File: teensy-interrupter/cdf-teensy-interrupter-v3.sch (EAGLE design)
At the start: 42 parts, among them IC1 TP4056, Q1 BC817-40LT1SMD

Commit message: More work
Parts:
- removed MIDI, PULSE: 100SP1T1B4M2QE, keves:100SP1T1B4M2QE
- removed PULSE_DUTY, PULSE_WIDTH: 10K PTV09A-4025F-B103, Bourns:POTENTIOMETERPTV09A_VERTICAL
- removed SW1: (no value), adafruit:DPDT-EG1390
- added D1, D3: 1A/23V/620mV, SparkFun-DiscreteSemi:DIODE-SCHOTTKY-BAT20J
- added PWR: 100SP1T1B4M2QE, keves:100SP1T1B4M2QE
- added R12: 50000, rcl:R-US_R0805
- added R13: 100000, rcl:R-US_R0805
- added S1: ENCODER-2LED, SparkFun-Switches:ENCODER-2LED
- R3, R5: value 330 -> 100
- R7: value 68 -> 27
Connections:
- net RX renamed MIDI_RX
- removed net PULSE_DUTY: PULSE_DUTY.WIPER, U$1.15/A1/T
- removed net PULSE_WIDTH: PULSE_WIDTH.WIPER, U$1.14/A1
- removed net TX2: U$1.22/A8/T/PWM
- removed net TX3: U$1.23/A9/T/PWM
- new net ENC_A: S1.A, U$1.14/A1
- new net ENC_B: S1.B, U$1.15/A1/T
- new net ENC_Z: S1.SW, U$1.16/A2/T
- new net N$23: B+.1, D3.A, IC1.BAT
- new net V_SENSE: R12.1, R13.2
- net +3V3: now also R5.2, S1.C, U$3.VDD; no longer MIDI.1, PULSE.1, PULSE_DUTY.CW, PULSE_WIDTH.CW
- net +5V: now also VR1.CCW; no longer R3.2, R5.2, R7.2, U$3.VDD, VR1.CW
- net GND: now also R13.1, VR1.CW; no longer MIDI.3, PULSE.3, PULSE_DUTY.CCW, PULSE_WIDTH.CCW, VR1.CCW
- net MIDI_MODE: no longer MIDI.2
- net N$20: now also D1.C, D3.C, PWR.2; no longer B+.1, IC1.BAT, SW11.S, SW12.O
- net N$22: now also D1.A, VUSB.1; no longer SW11.P
- net N$24: now also R3.2, R7.2; no longer SW11.O, SW12.S, VUSB.1
- net PULSE_MODE: no longer PULSE.2
- net V+: now also PWR.3, R12.2; no longer SW12.P
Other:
- moved on the sheet: B+, B-, C1, C2, C3, CHARGED, CHARGING, D2, EMERGENCY, IC1, LED_POWER, LED_TX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

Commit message: WIP?
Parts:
- removed B+, B-: (no value), adafruit:PINHD-1X1
- removed EMERGENCY: TL1105LF250Q, SparkFun-Electromechanical:SWITCH-MOMENTARY-2PTH
- removed R4: 220, rcl:R-US_0204/7
- removed U$3: LCD-HD447804-HOLES16X2-4-HOLES, HD44780LCD:LCD-HD447804-HOLES16X2-4-HOLES
- removed VR1: 10k, SparkFun-Resistors:TRIMPOT-PTH-10MM-KNOB-1/2W-10%
- added BATT, ESTOP: (no value), pinhead:PINHD-1X2
- added R14, R15: 100, rcl:R-US_R0805
- added SCRN: (no value), adafruit:PINHD-1X3
- renumbered U$1 to TEENSY, U$4 to MIDI
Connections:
- removed net +5V: R4.1, VR1.CCW
- removed net LCD_D4: TEENSY.5/PWM, U$3.DB4
- removed net LCD_D5: TEENSY.6/PWM, U$3.DB5
- removed net LCD_D6: TEENSY.7/RX3, U$3.DB6
- removed net LCD_D7: TEENSY.8/TX3, U$3.DB7
- removed net LCD_EN: TEENSY.4/CAN-RX-PWM, U$3.E
- removed net LCD_RS: TEENSY.3/CAN-TX/PWM, U$3.RS
- removed net MIDI_MODE: TEENSY.10/TX2/PWM
- removed net N$23: B+.1, D3.A, IC1.BAT
- removed net N$5: U$3.VO, VR1.WIPER
- removed net N$6: R4.2, U$3.A
- removed net PULSE_MODE: TEENSY.9/RX2/PWM
- new net B+: BATT.2, D3.A, IC1.BAT
- new net B+1: ESTOP.2
- new net IND_G: R15.1, TEENSY.17/A3/T
- new net IND_R: R14.1, TEENSY.18/A4/T/SDA0
- new net N$25: R15.2, S1.+G
- new net N$26: R14.2, S1.+R
- new net SCRN_TX: SCRN.1, TEENSY.1/TX1/T
- net +3V3: now also SCRN.3; no longer U$3.VDD
- net EMERGENCY: now also TEENSY.19/A5/T/SCL0; no longer EMERGENCY.1, TEENSY.11/MOSI
- net ENC_A: now also TEENSY.15/A1/T; no longer TEENSY.14/A1
- net ENC_B: now also TEENSY.14/A1; no longer TEENSY.15/A1/T
- net GND: now also BATT.1, ESTOP.1, SCRN.2; no longer B-.1, EMERGENCY.2, U$3.K, U$3.R/W, U$3.VSS, VR1.CW
- net V_SENSE: now also TEENSY.20/A6/PWM
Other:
- moved on the sheet: C1, CHARGED, CHARGING, D1, D2, D3, FB1, FB2, IC1, LED_TX, OPT1, Q1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

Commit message: v3 first press
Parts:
- removed D2: (no value), diode:DIODE-DO-214AC
- removed PWR: 100SP1T1B4M2QE, keves:100SP1T1B4M2QE
- added D4: 1A/23V/620mV, SparkFun-DiscreteSemi:DIODE-SCHOTTKY-BAT20J
- added POWER: (no value), pinhead:PINHD-1X2
- H1, H2, H3, H4: value MOUNT-HOLE3.3 -> MOUNT-PAD-ROUND3.0; device holes:MOUNT-HOLE3.3 -> holes:MOUNT-PAD-ROUND3.0
- renumbered LED_TX to TX1
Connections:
- net N$24 renamed 3.3V
- removed net B+1: ESTOP.2
- net EMERGENCY: now also ESTOP.2, TEENSY.5/PWM; no longer TEENSY.19/A5/T/SCL0
- net ENC_A: now also TEENSY.13/SCK/LED; no longer TEENSY.15/A1/T
- net GND: now also H1.MOUNT, H2.MOUNT, H3.MOUNT, H4.MOUNT
- net N$2: now also D4.C; no longer D2.C
- net N$20: now also POWER.1; no longer PWR.2
- net N$3: now also D4.A; no longer D2.A
- net V+: now also POWER.2; no longer PWR.3
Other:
- note removed: "TL1105LF250Q"
- moved on the sheet: BATT, ESTOP, H1, H2, H3, H4, R14, R15, S1, SCRN

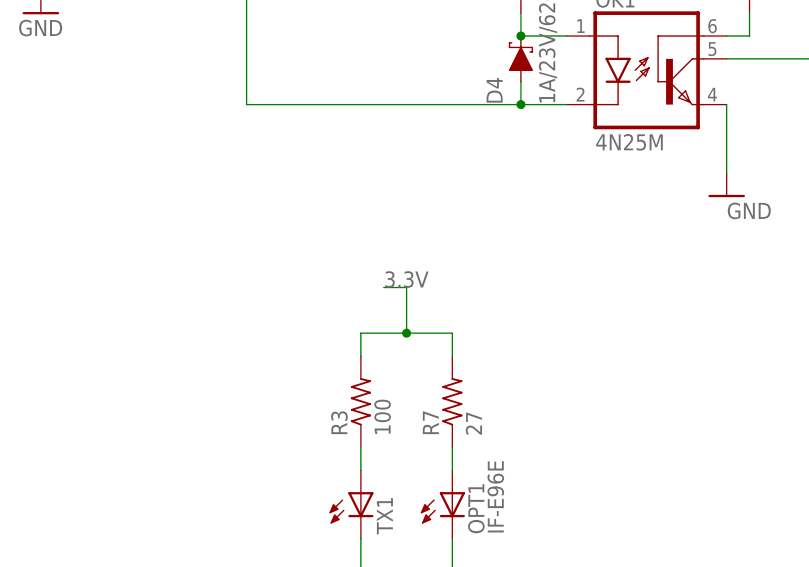
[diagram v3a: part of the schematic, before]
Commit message: Small board shrink
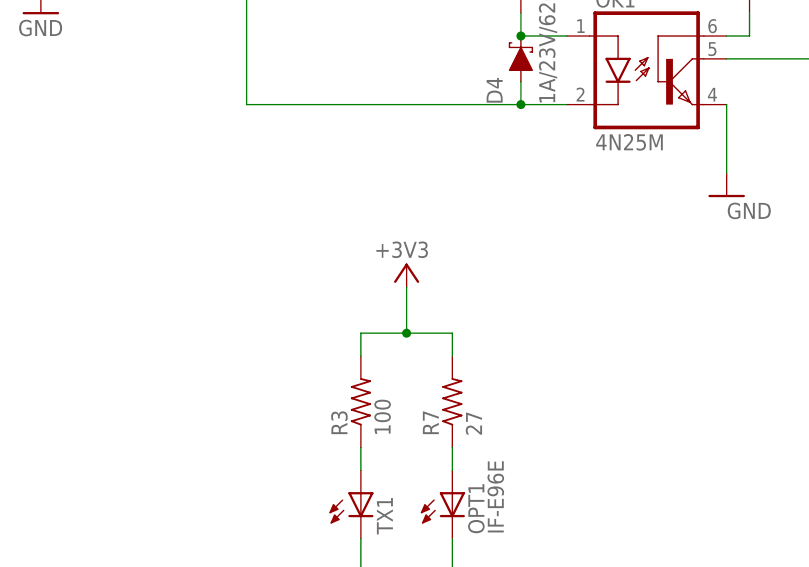
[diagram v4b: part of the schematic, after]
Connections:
- removed net 3.3V: R3.2, R7.2
- net +3V3: now also R3.2, R7.2
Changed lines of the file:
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@@
 <part name="H4" library="holes" library_urn="urn:adsk.eagle:library:237" deviceset="MOUNT-PAD-ROUND" device="3.0" package3d_urn="urn:adsk.eagle:package:14280/1"/>
 <part name="GND6" library="supply1" library_urn="urn:adsk.eagle:library:371" deviceset="GND" device=""/>
+<part name="+3V2" library="supply1" library_urn="urn:adsk.eagle:library:371" deviceset="+3V3" device=""/>
 </parts>
 <sheets>
@@
 <instance part="GND6" gate="1" x="-68.58" y="104.14" smashed="yes">
 <attribute name="VALUE" x="-71.12" y="101.6" size="1.778" layer="96"/>
+</instance>
+<instance part="+3V2" gate="G$1" x="-27.94" y="76.2" smashed="yes">
+<attribute name="VALUE" x="-25.4" y="78.74" size="1.778" layer="96" rot="R180"/>
 </instance>
 </instances>
@@
 <pinref part="+3V5" gate="G$1" pin="+3V3"/>
 <wire x1="170.18" y1="88.9" x2="170.18" y2="93.98" width="0.1524" layer="91"/>
+</segment>
+<segment>
+<wire x1="-22.86" y1="66.04" x2="-22.86" y2="68.58" width="0.1524" layer="91"/>
+<wire x1="-22.86" y1="68.58" x2="-27.94" y2="68.58" width="0.1524" layer="91"/>
+<wire x1="-27.94" y1="68.58" x2="-33.02" y2="68.58" width="0.1524" layer="91"/>
+<wire x1="-33.02" y1="68.58" x2="-33.02" y2="66.04" width="0.1524" layer="91"/>
+<pinref part="R3" gate="G$1" pin="2"/>
+<pinref part="R7" gate="G$1" pin="2"/>
+<pinref part="+3V2" gate="G$1" pin="+3V3"/>
+<wire x1="-27.94" y1="73.66" x2="-27.94" y2="68.58" width="0.1524" layer="91"/>
+<junction x="-27.94" y="68.58"/>
 </segment>
 </net>
@@
 </segment>
 </net>
-<net name="3.3V" class="0">
-<segment>
-<wire x1="-22.86" y1="66.04" x2="-22.86" y2="68.58" width="0.1524" layer="91"/>
-<wire x1="-22.86" y1="68.58" x2="-27.94" y2="68.58" width="0.1524" layer="91"/>
-<wire x1="-27.94" y1="68.58" x2="-33.02" y2="68.58" width="0.1524" layer="91"/>
-<wire x1="-33.02" y1="68.58" x2="-33.02" y2="66.04" width="0.1524" layer="91"/>
-<pinref part="R3" gate="G$1" pin="2"/>
-<pinref part="R7" gate="G$1" pin="2"/>
-<wire x1="-27.94" y1="68.58" x2="-27.94" y2="73.66" width="0.1524" layer="91"/>
-<wire x1="-27.94" y1="73.66" x2="-30.48" y2="73.66" width="0.1524" layer="91"/>
-<junction x="-27.94" y="68.58"/>
-<label x="-30.48" y="73.66" size="1.778" layer="95"/>
-</segment>
-</net>

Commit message: As printed
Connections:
- net GND: now also S1.-
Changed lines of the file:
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@@
 <part name="GND6" library="supply1" library_urn="urn:adsk.eagle:library:371" deviceset="GND" device=""/>
 <part name="+3V2" library="supply1" library_urn="urn:adsk.eagle:library:371" deviceset="+3V3" device=""/>
+<part name="GND7" library="supply1" library_urn="urn:adsk.eagle:library:371" deviceset="GND" device=""/>
 </parts>
 <sheets>
@@
 <instance part="+3V2" gate="G$1" x="-27.94" y="76.2" smashed="yes">
 <attribute name="VALUE" x="-25.4" y="78.74" size="1.778" layer="96" rot="R180"/>
+</instance>
+<instance part="GND7" gate="1" x="180.34" y="109.22" smashed="yes">
+<attribute name="VALUE" x="177.8" y="106.68" size="1.778" layer="96"/>
 </instance>
 </instances>
@@
 <pinref part="GND6" gate="1" pin="GND"/>
 </segment>
+<segment>
+<pinref part="S1" gate="G$1" pin="-"/>
+<pinref part="GND7" gate="1" pin="GND"/>
+<wire x1="177.8" y1="116.84" x2="180.34" y2="116.84" width="0.1524" layer="91"/>
+<wire x1="180.34" y1="116.84" x2="180.34" y2="111.76" width="0.1524" layer="91"/>
+</segment>
 </net>

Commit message: V3r1
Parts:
- removed R14, R15: 100, rcl:R-US_R0805
- removed S1: ENCODER-2LED, SparkFun-Switches:ENCODER-2LED
- added C4: 10uF, rcl:C-EUC0805
- added J2, J3: 4p-2.54, OPL_Connector:DIP-BLACK-MALE-HEADER-VERT(4P-2.54)
- added R16, R17: 100, rcl:R-US_R0805
- added R4: 10k, rcl:R-US_R0805
- R11: value 1.2K -> 10k
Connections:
- net N$20 renamed SW
- net N$22 renamed V_USB
- removed net N$25: R15.2, S1.+G
- removed net N$26: R14.2, S1.+R
- new net N$20: J2.P$3, R16.1
- new net N$5: J3.P$1, R4.2
- new net N$6: J2.P$2, R17.1
- net +3V3: now also R4.1; no longer S1.C
- net B+: now also C4.1
- net ENC_A: now also J3.P$2; no longer S1.A
- net ENC_B: now also J3.P$3; no longer S1.B
- net ENC_Z: now also J2.P$1; no longer S1.SW
- net GND: now also C4.2, J2.P$4; no longer S1.-
- net IND_G: now also R17.2; no longer R15.1
- net IND_R: now also R16.2; no longer R14.1
- net SCRN_TX: now also TEENSY.10/TX2/PWM; no longer TEENSY.1/TX1/T
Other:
- moved on the sheet: BATT

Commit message: WIP
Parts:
- renumbered LED_POWER to PWR
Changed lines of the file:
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@@
 <setting verticaltext="up"/>
 </settings>
-<grid distance="0.05" unitdist="inch" unit="inch" style="lines" multiple="1" display="no" altdistance="0.01" altunitdist="inch" altunit="inch"/>
+<grid distance="0.1" unitdist="inch" unit="inch" style="lines" multiple="1" display="no" altdistance="0.01" altunitdist="inch" altunit="inch"/>
 <layers>
 <layer number="1" name="Top" color="4" fill="1" visible="no" active="no"/>
@@
 <part name="Q1" library="transistor-npn" library_urn="urn:adsk.eagle:library:398" deviceset="BC817*" device="SMD" package3d_urn="urn:adsk.eagle:package:28748/2" technology="-40LT1"/>
 <part name="R5" library="rcl" library_urn="urn:adsk.eagle:library:334" deviceset="R-US_" device="R0805" package3d_urn="urn:adsk.eagle:package:23553/2" value="100"/>
-<part name="LED_POWER" library="adafruit" library_urn="urn:adsk.eagle:library:420" deviceset="LED" device="CHIP-LED0805" package3d_urn="urn:adsk.eagle:package:6240557/1"/>
+<part name="PWR" library="adafruit" library_urn="urn:adsk.eagle:library:420" deviceset="LED" device="CHIP-LED0805" package3d_urn="urn:adsk.eagle:package:6240557/1"/>
 <part name="TEENSY" library="Teensy_3_and_LC_Series_Boards_v1.1" deviceset="TEENSY_3.1_DIL" device=""/>
 <part name="IC1" library="TP4056" deviceset="TP4056" device=""/>
@@
 <attribute name="VALUE" x="115.062" y="72.39" size="1.778" layer="96" rot="R90"/>
 </instance>
-<instance part="LED_POWER" gate="G$1" x="111.76" y="63.5" smashed="yes">
+<instance part="PWR" gate="G$1" x="111.76" y="63.5" smashed="yes">
 <attribute name="NAME" x="115.316" y="53.848" size="1.778" layer="95" rot="R90"/>
 <attribute name="VALUE" x="117.475" y="58.928" size="1.778" layer="96" rot="R90"/>
@@
 <pinref part="GND12" gate="1" pin="GND"/>
 <wire x1="111.76" y1="55.88" x2="111.76" y2="58.42" width="0.1524" layer="91"/>
-<pinref part="LED_POWER" gate="G$1" pin="C"/>
+<pinref part="PWR" gate="G$1" pin="C"/>
 </segment>
 <segment>
@@
 <wire x1="111.76" y1="66.04" x2="111.76" y2="68.58" width="0.1524" layer="91"/>
 <pinref part="R5" gate="G$1" pin="1"/>
-<pinref part="LED_POWER" gate="G$1" pin="A"/>
-</segment>
-</net>
+<pinref part="PWR" gate="G$1" pin="A"/>
+</segment>
+</net>
